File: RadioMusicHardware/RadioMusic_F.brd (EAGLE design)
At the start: 107 x 19 mm, 31 parts, among them X1 VERT_SD_CARD_REV2

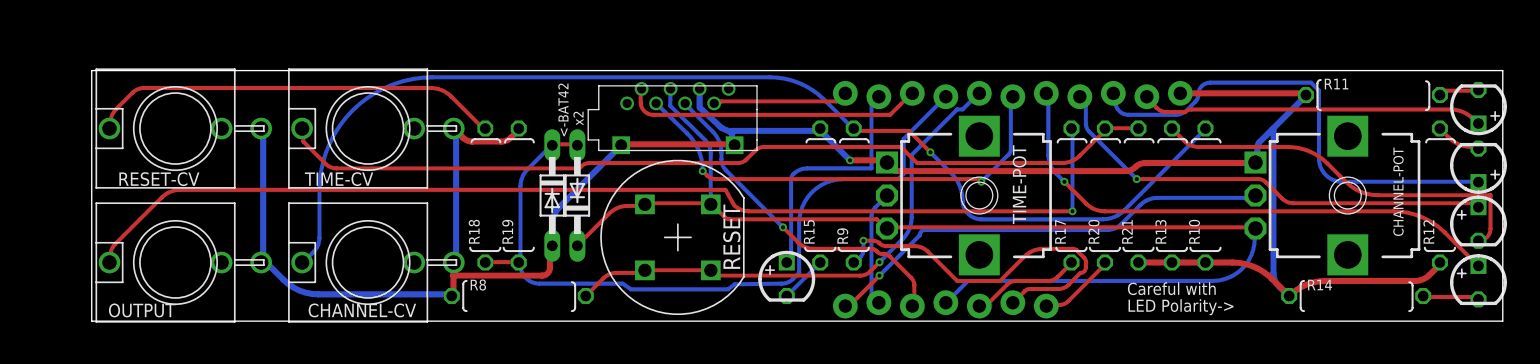
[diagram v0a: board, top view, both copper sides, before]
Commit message: Front board rerouting
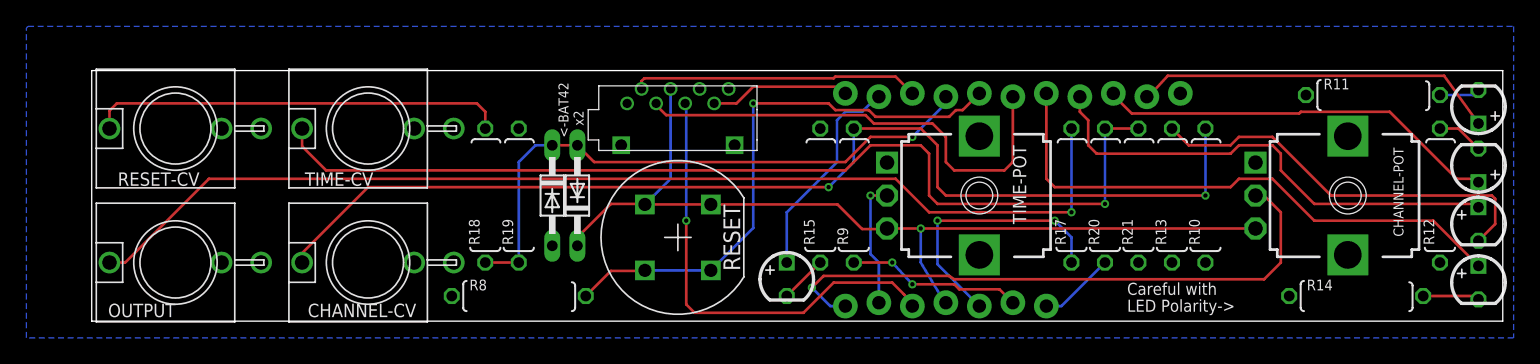
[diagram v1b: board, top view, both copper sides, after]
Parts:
- CHANNEL-CV, OUTPUT, RESET-CV, TIME-CV: value (none) -> THONKICONNNEW; device thonkiconn:WQP-PJ301M-12_JACK -> MusicThingModular:WQP-PJ301M-12_JACK
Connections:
- net GND_F: now also CHANNEL-CV.P$3_SLEEVE, OUTPUT.P$3_SLEEVE, RESET-CV.P$3_SLEEVE, TIME-CV.P$3_SLEEVE; no longer CHANNEL-CV.P$3, OUTPUT.P$3, RESET-CV.P$3, TIME-CV.P$3
- net N$14: now also RESET-CV.P$1_TIP; no longer RESET-CV.P$1
- net N$3: now also OUTPUT.P$1_TIP; no longer OUTPUT.P$1
- net N$9: now also CHANNEL-CV.P$1_TIP; no longer CHANNEL-CV.P$1
- net TEMP: now also TIME-CV.P$1_TIP; no longer TIME-CV.P$1
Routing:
- net GND_F: track 172.9 -> 0.00 mm, vias 1 -> 0
- net +3.3V_F: track 89.7 -> 69.9 mm, vias 0 -> 1
- net CHANNEL_CV_F: track 28.2 -> 13.4 mm, vias 1 -> 2
- net AUDIO_OUT_F: track 8.24 -> 20.4 mm, vias 0 -> 2
- net CHANNEL_POT_F: track 34.4 -> 45.9 mm
- net RESET_CV_F: track 57.3 -> 45.9 mm, vias 0 -> 1
- net SCLK_F: track 25.6 -> 34.5 mm
- net TEMP: track 67.1 -> 75.7 mm, vias 0 -> 1
- net LED2_F: track 35.9 -> 30.7 mm
- net RESET_SW_F: track 39.6 -> 42.6 mm
- net LED_RESET_F: track 18.6 -> 16.3 mm
- net LED3_F: track 34.6 -> 36.8 mm, vias 1 -> 0
- net LED1_F: track 25.9 -> 27.7 mm
- net LED4_F: track 40.8 -> 42.5 mm, vias 1 -> 0
- net N$20: track 29.5 -> 30.9 mm
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- added copper zone on layer 16, net GND_F

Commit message: Front panel revision & routing
Change input resistors re: #78 - improved routing with ground plane
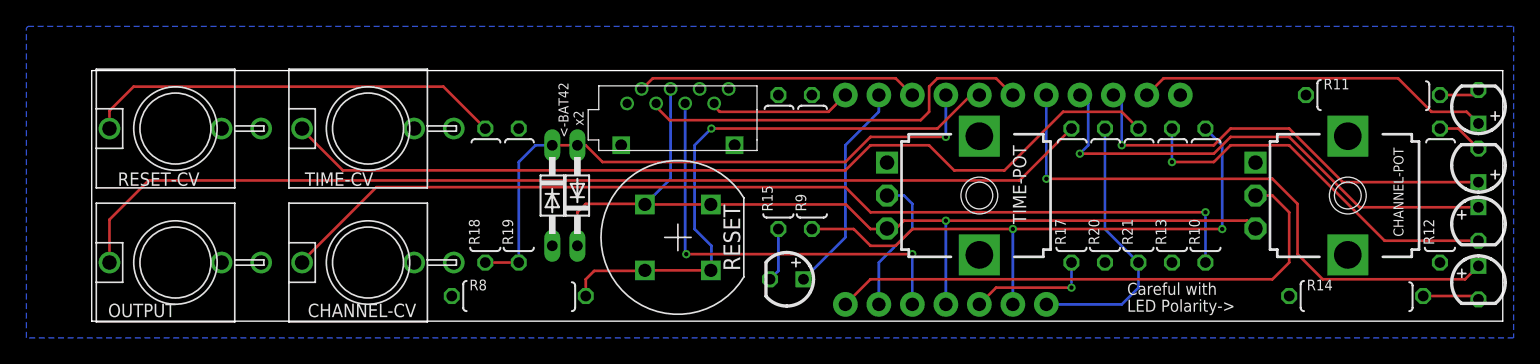
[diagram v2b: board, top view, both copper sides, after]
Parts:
- JP2: value M11LOCK -> M11PTH; device SparkFun-Connectors:1X11_LOCK -> SparkFun-Connectors:1X11
- JP4: device SparkFun-Connectors:1X07_LOCK -> SparkFun-Connectors:1X07
- R10, R21: value 47k -> 22k
- R20, R9: value 22k -> 47k
- moved R15 4.07 mm to (52.1, 12.1)
- moved R9 4.07 mm to (54.6, 12.1)
- turned LED5 to 180 degrees
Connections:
- removed net N$9: CHANNEL-CV.P$1_TIP, R10.2, R9.2
- removed net TEMP: R20.2, R21.2, TIME-CV.P$1_TIP
- new net N$1: CHANNEL-CV.P$1_TIP, R10.1
- new net N$2: R21.2, TIME-CV.P$1_TIP
- net CHANNEL_CV_F: now also R10.2
- net GND_F: now also R20.1, R9.2; no longer R10.1, R21.1
- net TIME_CV_F: now also R20.2, R21.1; no longer R20.1
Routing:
- net N$9: track 83.7 -> 0.00 mm, vias 2 -> 0
- net TEMP: track 75.7 -> 0.00 mm, vias 1 -> 0
- net N$1: track 0.00 -> 75.5 mm, vias 0 -> 1
- net N$2: track 0.00 -> 68.7 mm
- net CHANNEL_CV_F: track 13.4 -> 46.0 mm
- net TIME_CV_F: track 5.81 -> 20.6 mm
- net AUDIO_OUT_F: track 20.4 -> 9.42 mm, vias 2 -> 1
- net MOSI_F: track 35.6 -> 30.7 mm
- net CHANNEL_POT_F: track 45.9 -> 41.9 mm, vias 1 -> 0
- net N$3: track 83.0 -> 79.1 mm, vias 1 -> 0
- net LED2_F: track 30.7 -> 33.3 mm, vias 0 -> 1
- net LED4_F: track 42.5 -> 44.9 mm, vias 0 -> 1
- net SCLK_F: track 34.5 -> 32.4 mm, vias 1 -> 2
- net +3.3V_F: track 69.9 -> 71.5 mm
- net RESET_SW_F: track 42.6 -> 44.2 mm
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
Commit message: Revision 3 front and back PCBs sent to Fab
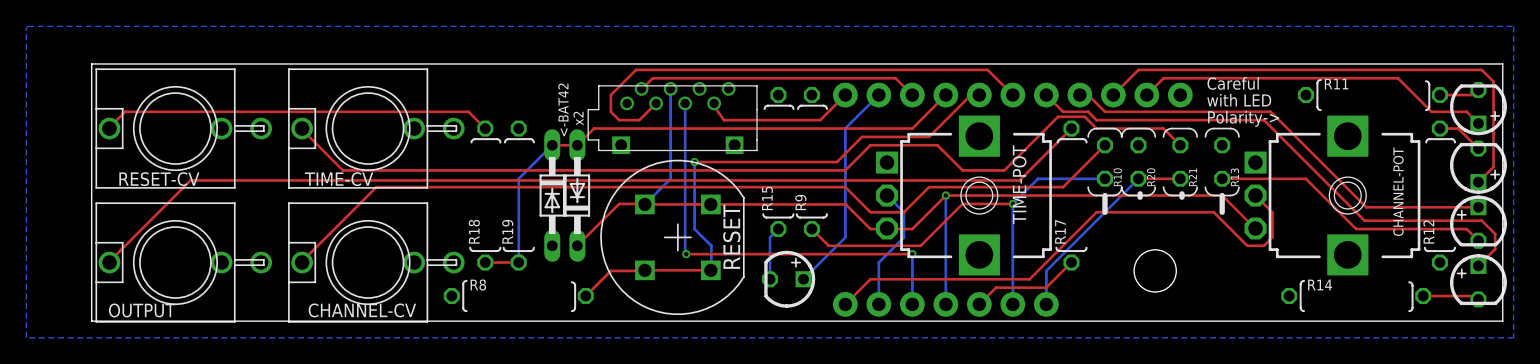
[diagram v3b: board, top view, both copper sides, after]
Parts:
- removed U$1: (no value), TW_logos:MTM_2CM
- added U$2: (no value), MusicThingModular:MOUNTING_HOLE
- R10, R13, R20, R21: device TomW:0207/10 -> MusicThingModular:VERTICAL_RESISTOR
- moved R10 8.03 mm to (76.8, 12.1)
- moved R13 4.58 mm to (85.7, 12.1)
- moved R21 4.07 mm to (82.5, 12.1)
- moved R20 3.59 mm to (79.4, 12.1)
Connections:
- net CHANNEL_CV_F: now also R10.1; no longer R10.2
- net GND_F: now also R13.2, R20.2; no longer R13.1, R20.1
- net N$1: now also R10.2; no longer R10.1
- net N$20: now also R13.1; no longer R13.2
- net TIME_CV_F: now also R20.1; no longer R20.2
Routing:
- net CHANNEL_CV_F: track 46.0 -> 32.5 mm, vias 2 -> 1
- net N$1: track 75.5 -> 66.2 mm, vias 1 -> 0
- net N$20: track 29.3 -> 21.4 mm, vias 1 -> 0
- net MOSI_F: track 30.7 -> 37.5 mm
- net TIME_CV_F: track 20.6 -> 15.6 mm
- net LED2_F: track 33.3 -> 38.1 mm, vias 1 -> 0
- net LED3_F: track 37.9 -> 33.8 mm, vias 1 -> 0
- net RESET_CV_F: track 47.6 -> 43.9 mm, vias 1 -> 0
- net LED4_F: track 44.9 -> 41.3 mm, vias 1 -> 0
- net N$2: track 68.7 -> 72.1 mm
- net N$14: track 31.9 -> 29.6 mm
- net +3.3V_F: track 71.5 -> 73.6 mm
- net N$3: track 79.1 -> 77.2 mm
- net CHANNEL_POT_F: track 41.9 -> 40.3 mm
- net RESET_SW_F: track 44.2 -> 42.7 mm
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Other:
- board size 107 x 19 mm -> 107 x 19.5 mm
- board text added: "Radio Music Front PCB rev 3 Designed in Herne Hill, London by Tom Whitwell November 2015 CC-BY-SA musicthing.co.uk"
- board text removed: "Radio Music Front PCB rev 2.1 Designed in Herne Hill, London by Tom Whitwell February 2015 CC-BY-SA musicthing.co.uk"

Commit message: 3.1 Hardware Finalised
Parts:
- R11, R12, R14, R15, R17, R18, R19, R8, R9: device TomW:0207/10 -> MusicThingModular:7MM_RESISTOR
- moved R11 0.64 mm to (97.8, 17.1)
- moved R15 0.63 mm to (52.1, 11.4)
- moved R17 0.63 mm to (74.3, 10.2)
- moved R9 0.63 mm to (54.6, 11.4)
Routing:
- net MISO_F: track 11.5 -> 14.2 mm
- net N$21: track 4.30 -> 5.57 mm
- net RESET_SW_F: track 42.7 -> 44.0 mm
- net N$14: track 29.6 -> 30.9 mm
- net AUDIO_OUT_F: track 8.30 -> 9.09 mm
- net N$18: track 3.08 -> 3.71 mm
- net N$25: track 4.07 -> 4.71 mm
- net +3.3V_F: track 73.6 -> 74.1 mm
- net N$19: track 3.55 -> 3.03 mm
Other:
- board text added: "Radio Music Front PCB rev 3.1 Designed in Herne Hill, London by Tom Whitwell November 2015 CC-BY-SA musicthing.co.uk"
- board text removed: "Radio Music Front PCB rev 3 Designed in Herne Hill, London by Tom Whitwell November 2015 CC-BY-SA musicthing.co.uk"

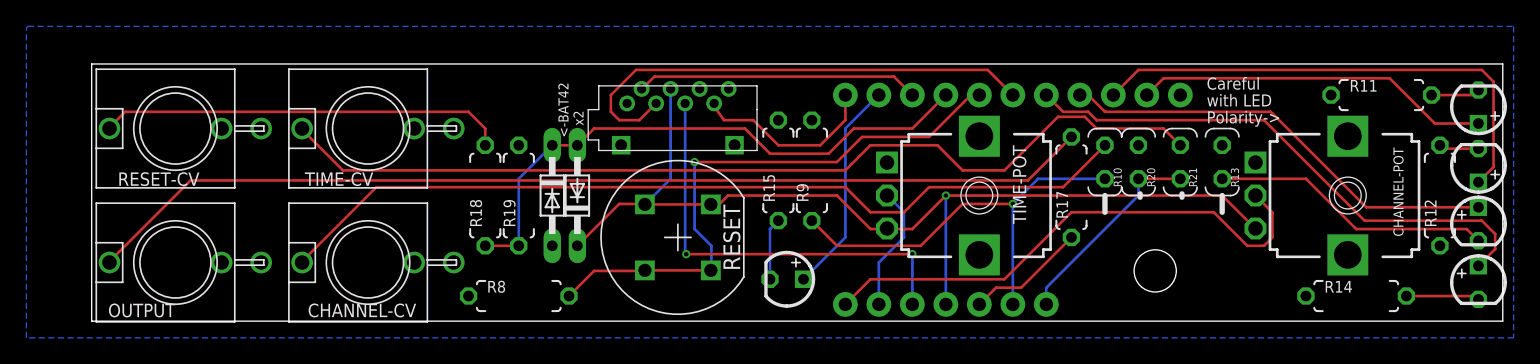
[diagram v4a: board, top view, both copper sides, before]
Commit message: Routed Version 2 -  needs to be checked
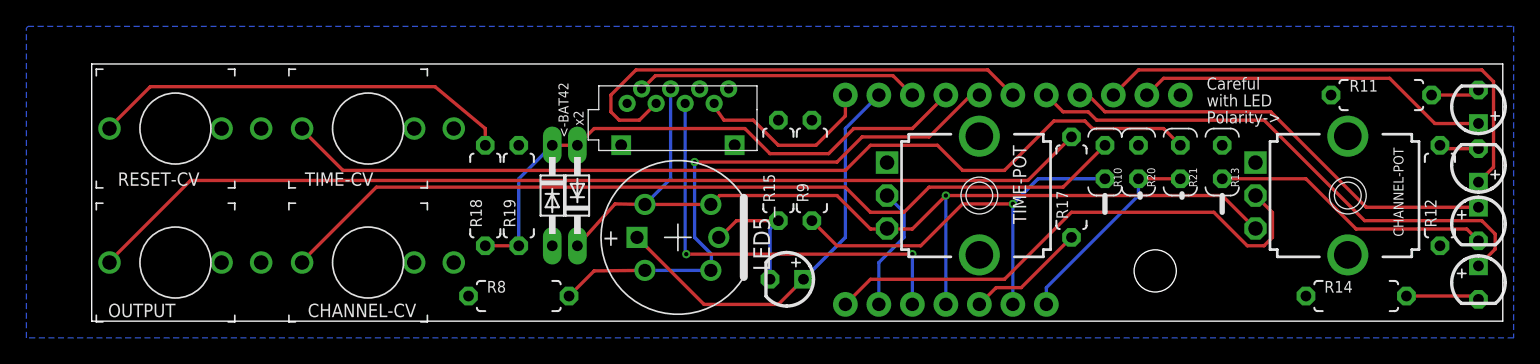
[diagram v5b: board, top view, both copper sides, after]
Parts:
- removed RESET: D6_PUSH_SWITCH, TomW:D6_BUTTON_RND
- added LED5_: D6-ILLUM, MusicThingModular:D6_PUSH_SWITCH_ILLUM
- R10, R21: value 22k -> 27k
- R17, R18: value 220R -> 470r
- R20, R9: value 47k -> 56k
- R8: value 10k -> 27k
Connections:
- net +3.3V_F: now also LED5_.P$3, LED5_.P$4; no longer RESET.P$3, RESET.P$4
- net LED_RESET_F: now also LED5_.LED+
- net N$25: now also LED5_.LED-
- net RESET_SW_F: now also LED5_.P$1, LED5_.P$2; no longer RESET.P$1, RESET.P$2
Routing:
- net LED_RESET_F: track 16.3 -> 31.9 mm
- net N$25: track 4.71 -> 9.75 mm
- net N$14: track 30.9 -> 32.3 mm
